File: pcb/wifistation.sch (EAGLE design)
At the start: 6 parts

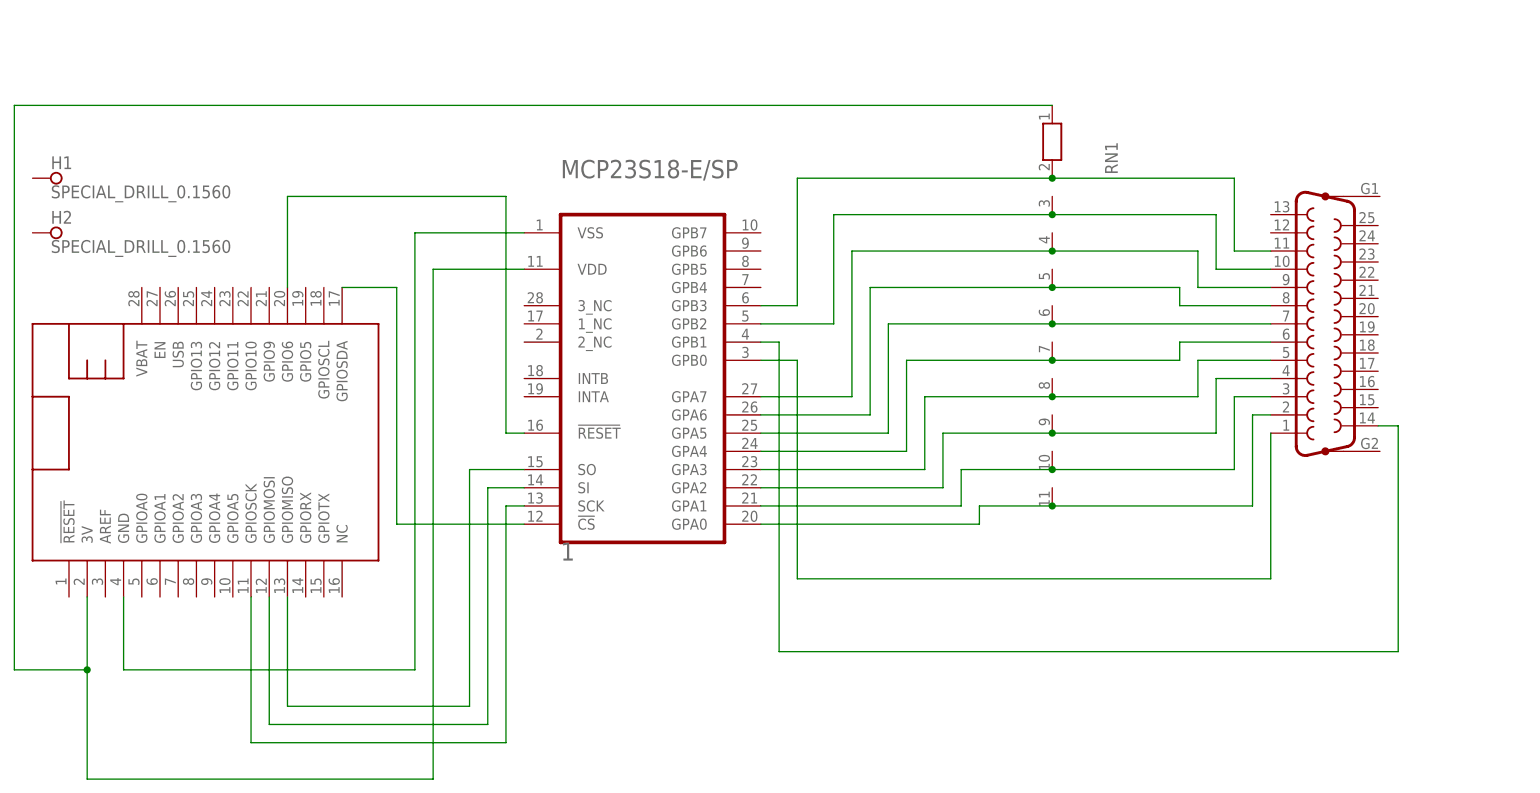
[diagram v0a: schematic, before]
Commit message: pcb: Add revision B, which fixes the pinout of the DB25 connector
The pinout of the d-sub part in Eagle was backwards from how I was
using it :(
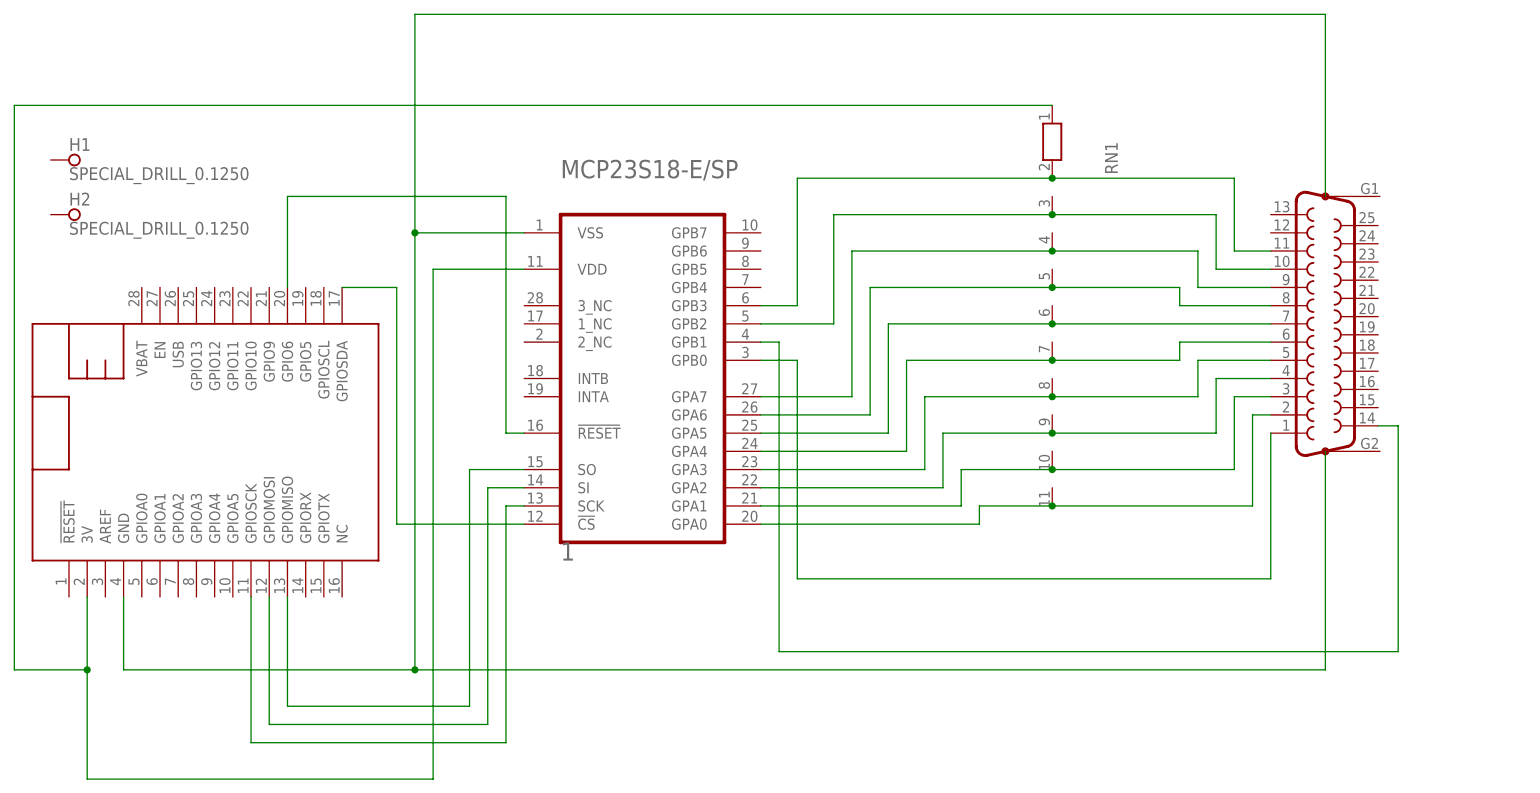
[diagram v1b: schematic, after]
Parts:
- H1, H2: value SPECIAL_DRILL_0.1560 -> SPECIAL_DRILL_0.1250; device special-drill:SPECIAL_DRILL_0.1560 -> special-drill:SPECIAL_DRILL_0.1250
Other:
- moved on the sheet: H1, H2
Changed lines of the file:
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@@
 <layers>
 <layer number="1" name="Top" color="4" fill="1" visible="no" active="no"/>
+<layer number="2" name="Route2" color="1" fill="3" visible="no" active="no"/>
+<layer number="3" name="Route3" color="4" fill="3" visible="no" active="no"/>
+<layer number="4" name="Route4" color="1" fill="4" visible="no" active="no"/>
+<layer number="5" name="Route5" color="4" fill="4" visible="no" active="no"/>
+<layer number="6" name="Route6" color="1" fill="8" visible="no" active="no"/>
+<layer number="7" name="Route7" color="4" fill="8" visible="no" active="no"/>
+<layer number="8" name="Route8" color="1" fill="2" visible="no" active="no"/>
+<layer number="9" name="Route9" color="4" fill="2" visible="no" active="no"/>
+<layer number="10" name="Route10" color="1" fill="7" visible="no" active="no"/>
+<layer number="11" name="Route11" color="4" fill="7" visible="no" active="no"/>
+<layer number="12" name="Route12" color="1" fill="5" visible="no" active="no"/>
+<layer number="13" name="Route13" color="4" fill="5" visible="no" active="no"/>
+<layer number="14" name="Route14" color="1" fill="6" visible="no" active="no"/>
+<layer number="15" name="Route15" color="4" fill="6" visible="no" active="no"/>
 <layer number="16" name="Bottom" color="1" fill="1" visible="no" active="no"/>
 <layer number="17" name="Pads" color="2" fill="1" visible="no" active="no"/>
@@
 <part name="RN1" library="resistor-net" library_urn="urn:adsk.eagle:library:343" deviceset="RN10" device="" package3d_urn="urn:adsk.eagle:package:24979/1"/>
 <part name="FEATHER" library="jcs" deviceset="FEATHERWING" device="_NODIM_NOHOLES" package3d_urn="urn:adsk.eagle:package:6240960/1"/>
-<part name="H1" library="special-drill" library_urn="urn:adsk.eagle:library:366" deviceset="SPECIAL_DRILL_" device="0.1560" package3d_urn="urn:adsk.eagle:package:26543/1"/>
-<part name="H2" library="special-drill" library_urn="urn:adsk.eagle:library:366" deviceset="SPECIAL_DRILL_" device="0.1560" package3d_urn="urn:adsk.eagle:package:26543/1"/>
+<part name="H1" library="special-drill" library_urn="urn:adsk.eagle:library:366" deviceset="SPECIAL_DRILL_" device="0.1250" package3d_urn="urn:adsk.eagle:package:26538/1" value="SPECIAL_DRILL_0.1250"/>
+<part name="H2" library="special-drill" library_urn="urn:adsk.eagle:library:366" deviceset="SPECIAL_DRILL_" device="0.1250" package3d_urn="urn:adsk.eagle:package:26538/1" value="SPECIAL_DRILL_0.1250"/>
 </parts>
 <sheets>
@@
 </instance>
 <instance part="FEATHER" gate="G$1" x="5.08" y="35.56" smashed="yes"/>
-<instance part="H1" gate="G$1" x="7.62" y="88.9" smashed="yes">
-<attribute name="NAME" x="7.62" y="90.17" size="1.778" layer="95"/>
-<attribute name="VALUE" x="7.62" y="86.106" size="1.778" layer="96"/>
-</instance>
-<instance part="H2" gate="G$1" x="7.62" y="81.28" smashed="yes">
-<attribute name="NAME" x="7.62" y="82.55" size="1.778" layer="95"/>
-<attribute name="VALUE" x="7.62" y="78.486" size="1.778" layer="96"/>
+<instance part="H1" gate="G$1" x="10.16" y="91.44" smashed="yes">
+<attribute name="NAME" x="10.16" y="92.71" size="1.778" layer="95"/>
+<attribute name="VALUE" x="10.16" y="88.646" size="1.778" layer="96"/>
+</instance>
+<instance part="H2" gate="G$1" x="10.16" y="83.82" smashed="yes">
+<attribute name="NAME" x="10.16" y="85.09" size="1.778" layer="95"/>
+<attribute name="VALUE" x="10.16" y="81.026" size="1.778" layer="96"/>
 </instance>
 </instances>
@@
 <wire x1="17.78" y1="20.32" x2="17.78" y2="30.48" width="0.1524" layer="91"/>
 <pinref part="FEATHER" gate="G$1" pin="GND"/>
+<wire x1="58.42" y1="81.28" x2="58.42" y2="111.76" width="0.1524" layer="91"/>
+<junction x="58.42" y="81.28"/>
+<wire x1="58.42" y1="111.76" x2="185.42" y2="111.76" width="0.1524" layer="91"/>
+<wire x1="185.42" y1="111.76" x2="185.42" y2="86.36" width="0.1524" layer="91"/>
+<wire x1="58.42" y1="20.32" x2="185.42" y2="20.32" width="0.1524" layer="91"/>
+<junction x="58.42" y="20.32"/>
+<wire x1="185.42" y1="20.32" x2="185.42" y2="50.8" width="0.1524" layer="91"/>
 </segment>
 </net>

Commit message: pcb: Add revision C which grounds the DB25 mounts and pins 18-25
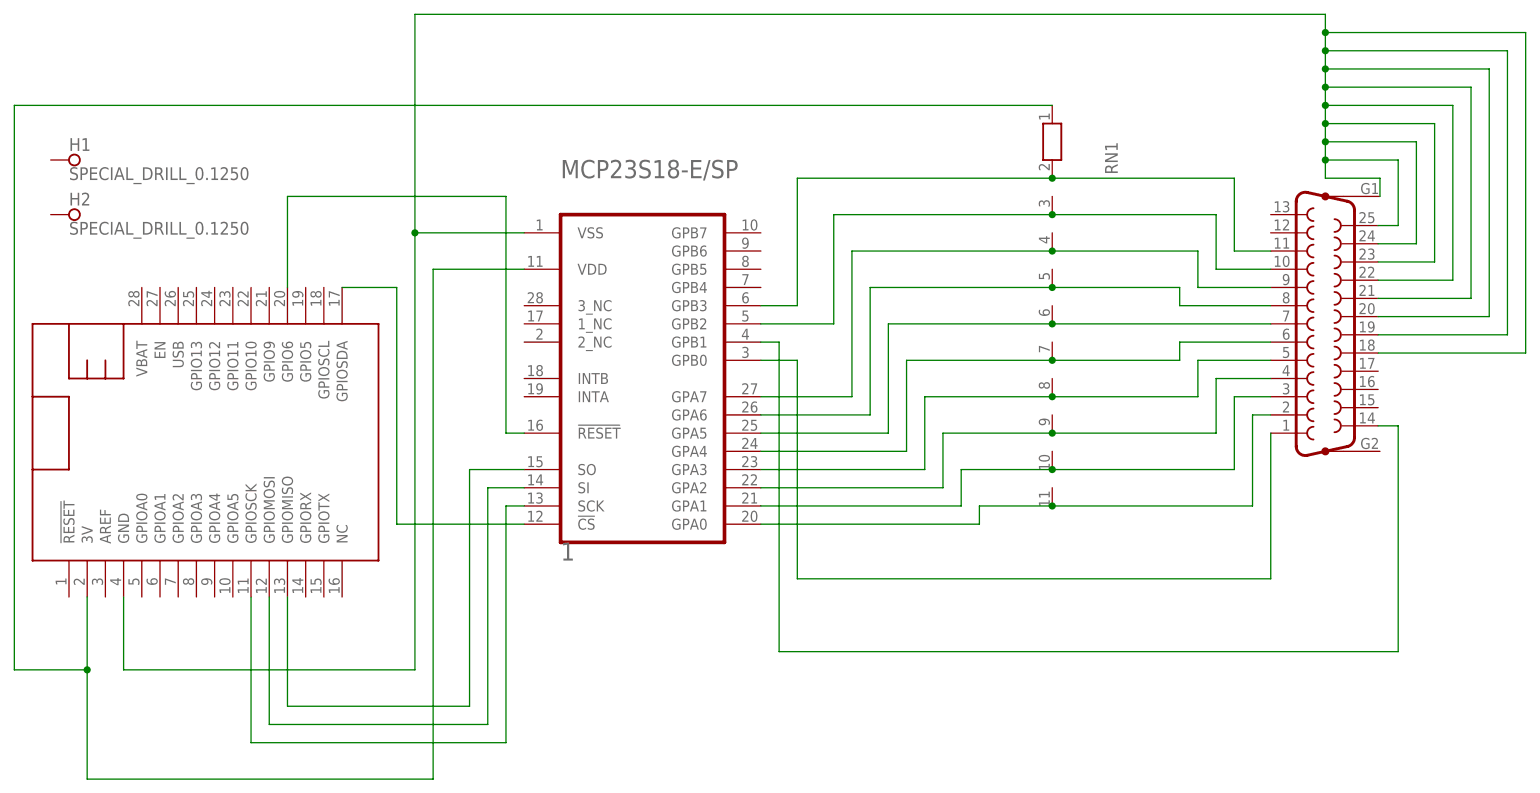
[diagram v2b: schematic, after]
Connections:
- net N$1: now also DB25.18, DB25.19, DB25.20, DB25.21, DB25.22, DB25.23, DB25.24, DB25.25, DB25.G1
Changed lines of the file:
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@@
 <junction x="58.42" y="81.28"/>
 <wire x1="58.42" y1="111.76" x2="185.42" y2="111.76" width="0.1524" layer="91"/>
-<wire x1="185.42" y1="111.76" x2="185.42" y2="86.36" width="0.1524" layer="91"/>
-<wire x1="58.42" y1="20.32" x2="185.42" y2="20.32" width="0.1524" layer="91"/>
-<junction x="58.42" y="20.32"/>
-<wire x1="185.42" y1="20.32" x2="185.42" y2="50.8" width="0.1524" layer="91"/>
+<wire x1="185.42" y1="111.76" x2="185.42" y2="109.22" width="0.1524" layer="91"/>
+<wire x1="185.42" y1="109.22" x2="185.42" y2="106.68" width="0.1524" layer="91"/>
+<wire x1="185.42" y1="106.68" x2="185.42" y2="104.14" width="0.1524" layer="91"/>
+<wire x1="185.42" y1="104.14" x2="185.42" y2="101.6" width="0.1524" layer="91"/>
+<wire x1="185.42" y1="101.6" x2="185.42" y2="99.06" width="0.1524" layer="91"/>
+<wire x1="185.42" y1="99.06" x2="185.42" y2="96.52" width="0.1524" layer="91"/>
+<wire x1="185.42" y1="96.52" x2="185.42" y2="93.98" width="0.1524" layer="91"/>
+<wire x1="185.42" y1="93.98" x2="185.42" y2="91.44" width="0.1524" layer="91"/>
+<wire x1="185.42" y1="91.44" x2="185.42" y2="88.9" width="0.1524" layer="91"/>
+<pinref part="DB25" gate="G$1" pin="25"/>
+<wire x1="192.786" y1="82.296" x2="195.58" y2="82.296" width="0.1524" layer="91"/>
+<wire x1="195.58" y1="82.296" x2="195.58" y2="91.44" width="0.1524" layer="91"/>
+<wire x1="195.58" y1="91.44" x2="185.42" y2="91.44" width="0.1524" layer="91"/>
+<junction x="185.42" y="91.44"/>
+<pinref part="DB25" gate="G$1" pin="24"/>
+<wire x1="192.786" y1="79.756" x2="198.12" y2="79.756" width="0.1524" layer="91"/>
+<wire x1="198.12" y1="79.756" x2="198.12" y2="93.98" width="0.1524" layer="91"/>
+<wire x1="198.12" y1="93.98" x2="185.42" y2="93.98" width="0.1524" layer="91"/>
+<junction x="185.42" y="93.98"/>
+<pinref part="DB25" gate="G$1" pin="23"/>
+<wire x1="192.786" y1="77.216" x2="200.66" y2="77.216" width="0.1524" layer="91"/>
+<wire x1="200.66" y1="77.216" x2="200.66" y2="96.52" width="0.1524" layer="91"/>
+<wire x1="200.66" y1="96.52" x2="185.42" y2="96.52" width="0.1524" layer="91"/>
+<junction x="185.42" y="96.52"/>
+<pinref part="DB25" gate="G$1" pin="22"/>
+<wire x1="192.786" y1="74.676" x2="203.2" y2="74.676" width="0.1524" layer="91"/>
+<wire x1="203.2" y1="74.676" x2="203.2" y2="99.06" width="0.1524" layer="91"/>
+<wire x1="203.2" y1="99.06" x2="185.42" y2="99.06" width="0.1524" layer="91"/>
+<junction x="185.42" y="99.06"/>
+<pinref part="DB25" gate="G$1" pin="21"/>
+<wire x1="192.786" y1="72.136" x2="205.74" y2="72.136" width="0.1524" layer="91"/>
+<wire x1="205.74" y1="72.136" x2="205.74" y2="101.6" width="0.1524" layer="91"/>
+<wire x1="205.74" y1="101.6" x2="185.42" y2="101.6" width="0.1524" layer="91"/>
+<junction x="185.42" y="101.6"/>
+<pinref part="DB25" gate="G$1" pin="20"/>
+<wire x1="192.786" y1="69.596" x2="208.28" y2="69.596" width="0.1524" layer="91"/>
+<wire x1="208.28" y1="69.596" x2="208.28" y2="104.14" width="0.1524" layer="91"/>
+<wire x1="208.28" y1="104.14" x2="185.42" y2="104.14" width="0.1524" layer="91"/>
+<junction x="185.42" y="104.14"/>
+<pinref part="DB25" gate="G$1" pin="19"/>
+<wire x1="192.786" y1="67.056" x2="210.82" y2="67.056" width="0.1524" layer="91"/>
+<wire x1="210.82" y1="67.056" x2="210.82" y2="106.68" width="0.1524" layer="91"/>
+<wire x1="210.82" y1="106.68" x2="185.42" y2="106.68" width="0.1524" layer="91"/>
+<junction x="185.42" y="106.68"/>
+<pinref part="DB25" gate="G$1" pin="18"/>
+<wire x1="192.786" y1="64.516" x2="213.36" y2="64.516" width="0.1524" layer="91"/>
+<wire x1="213.36" y1="64.516" x2="213.36" y2="109.22" width="0.1524" layer="91"/>
+<wire x1="213.36" y1="109.22" x2="185.42" y2="109.22" width="0.1524" layer="91"/>
+<junction x="185.42" y="109.22"/>
+<pinref part="DB25" gate="G$1" pin="G1"/>
+<wire x1="193.04" y1="86.36" x2="193.04" y2="88.9" width="0.1524" layer="91"/>
+<wire x1="193.04" y1="88.9" x2="185.42" y2="88.9" width="0.1524" layer="91"/>
 </segment>
 </net>
